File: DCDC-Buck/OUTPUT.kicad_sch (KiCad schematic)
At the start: 3 parts, among them CN2 STLZ950GH

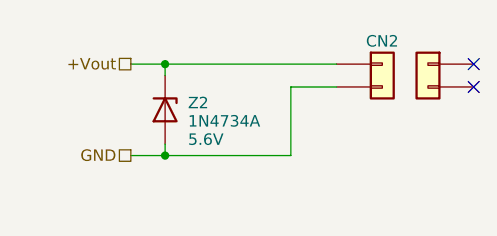
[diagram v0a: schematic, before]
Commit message: Finishing PCB design with 2 layers.
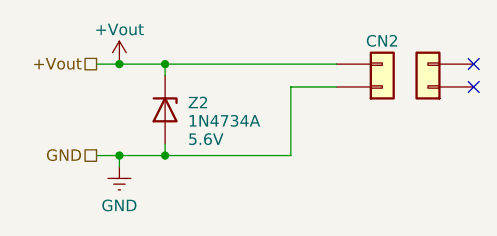
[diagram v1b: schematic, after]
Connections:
- net +Vout: now also CN2.2 (Pin_2); no longer CN2.1 (Pin_1)
- net GND: now also CN2.1 (Pin_1); no longer CN2.2 (Pin_2)
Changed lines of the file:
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@@
 	(title_block
 		(title "OUTPUT")
+		(date "2026-09-27")
 		(rev "A")
 		(company "Author: Ygor K.")
+	)
+	(junction
+		(at 125.73 96.52)
+		(diameter 0)
+		(color 0 0 0 0)
+	)
+	(junction
+		(at 125.73 106.68)
+		(diameter 0)
+		(color 0 0 0 0)
 	)
 	(junction
@@
 	(wire
 		(pts
-			(xy 127 96.52) (xy 130.81 96.52)
+			(xy 125.73 106.68) (xy 130.81 106.68)
+		)
+		(stroke
+			(width 0)
+			(type default)
+		)
+	)
+	(wire
+		(pts
+			(xy 123.19 96.52) (xy 125.73 96.52)
 		)
 		(stroke
@@
 	(wire
 		(pts
-			(xy 127 106.68) (xy 130.81 106.68)
+			(xy 125.73 96.52) (xy 130.81 96.52)
+		)
+		(stroke
+			(width 0)
+			(type default)
+		)
+	)
+	(wire
+		(pts
+			(xy 123.19 106.68) (xy 125.73 106.68)
+		)
+		(stroke
+			(width 0)
+			(type default)
+		)
+	)
+	(wire
+		(pts
+			(xy 125.73 106.68) (xy 125.73 107.95)
 		)
 		(stroke
@@
 	(hierarchical_label "+Vout"
 		(shape passive)
-		(at 127 96.52 180)
+		(at 123.19 96.52 180)
 		(effects
 			(font
@@
 	(hierarchical_label "GND"
 		(shape passive)
-		(at 127 106.68 180)
+		(at 123.19 106.68 180)
 		(effects
 			(font
@@
 	)
 	(symbol
+		(lib_id "power:VCC")
+		(at 125.73 96.52 0)
+		(unit 1)
+		(body_style 1)
+		(exclude_from_sim no)
+		(in_bom yes)
+		(on_board yes)
+		(in_pos_files yes)
+		(dnp no)
+		(property "Reference" "#PWR028"
+			(at 125.73 100.33 0)
+			(hide yes)
+			(show_name no)
+			(do_not_autoplace no)
+			(effects
+				(font
+					(size 1.27 1.27)
+				)
+			)
+		)
+		(property "Value" "+Vout"
+			(at 125.73 92.71 0)
+			(show_name no)
+			(do_not_autoplace no)
+			(effects
+				(font
+					(size 1.27 1.27)
+				)
+			)
+		)
+		(property "Footprint" ""
+			(at 125.73 96.52 0)
+			(hide yes)
+			(show_name no)
+			(do_not_autoplace no)
+			(effects
+				(font
+					(size 1.27 1.27)
+				)
+			)
+		)
+		(property "Datasheet" ""
+			(at 125.73 96.52 0)
+			(hide yes)
+			(show_name no)
+			(do_not_autoplace no)
+			(effects
+				(font
+					(size 1.27 1.27)
+				)
+			)
+		)
+		(property "Description" "Power symbol creates a global label with name \"VCC\""
+			(at 125.73 96.52 0)
+			(hide yes)
+			(show_name no)
+			(do_not_autoplace no)
+			(effects
+				(font
+					(size 1.27 1.27)
+				)
+			)
+		)
+		(pin "1"
+		)
+		(instances
+			(project "DCDC-Buck"
+				(path "/959e3d1c-01d0-4c7d-bf19-165b598aa596/74582b42-0ce4-4cfd-893d-1b8aeecfe42a"
+					(reference "#PWR028")
+					(unit 1)
+				)
+			)
+		)
+	)
+	(symbol
 		(lib_id "Connector_Generic:Conn_01x02")
-		(at 154.94 96.52 0)
+		(at 154.94 99.06 0)
+		(mirror x)
 		(unit 1)
 		(body_style 1)
@@
 		)
 		(property "Value" "STLZ950GH"
-			(at 154.94 102.108 0)
+			(at 154.94 93.472 0)
 			(hide yes)
 			(show_name no)
@@
 		)
 		(property "Footprint" "TerminalBlock_Phoenix:TerminalBlock_Phoenix_MKDS-1,5-2-5.08_1x02_P5.08mm_Horizontal"
-			(at 154.94 96.52 0)
+			(at 154.94 99.06 0)
 			(hide yes)
 			(show_name no)
@@
 		)
 		(property "Datasheet" ""
-			(at 154.94 96.52 0)
+			(at 154.94 99.06 0)
 			(hide yes)
 			(show_name no)
@@
 		)
 		(property "Description" "Conector Verde Multipolar STLZ950GH Macho 90º (Horizontal) Com as Laterais Fechadas - Passo 5,08mm"
-			(at 154.94 96.52 0)
+			(at 154.94 99.06 0)
 			(hide yes)
 			(show_name no)
@@
 		)
 		(property "Link" "https://www.multcomercial.com.br/conector-verde-multipolar-stlz950gh-macho-90-horizontal-com-as-laterais-fechadas-passo-5-08mm-2-a-18-vias-phoenix-mecano.html"
-			(at 154.94 96.52 0)
+			(at 154.94 99.06 0)
 			(hide yes)
 			(show_name no)
@@
 				(path "/959e3d1c-01d0-4c7d-bf19-165b598aa596/74582b42-0ce4-4cfd-893d-1b8aeecfe42a"
 					(reference "CN2")
+					(unit 1)
+				)
+			)
+		)
+	)
+	(symbol
+		(lib_id "power:GNDREF")
+		(at 125.73 107.95 0)
+		(unit 1)
+		(body_style 1)
+		(exclude_from_sim no)
+		(in_bom yes)
+		(on_board yes)
+		(in_pos_files yes)
+		(dnp no)
+		(property "Reference" "#PWR048"
+			(at 125.73 114.3 0)
+			(hide yes)
+			(show_name no)
+			(do_not_autoplace no)
+			(effects
+				(font
+					(size 1.27 1.27)
+				)
+			)
+		)
+		(property "Value" "GND"
+			(at 125.73 112.268 0)
+			(show_name no)
+			(do_not_autoplace no)
+			(effects
+				(font
+					(size 1.27 1.27)
+				)
+			)
+		)
+		(property "Footprint" ""
+			(at 125.73 107.95 0)
+			(hide yes)
+			(show_name no)
+			(do_not_autoplace no)
+			(effects
+				(font
+					(size 1.27 1.27)
+				)
+			)
+		)
+		(property "Datasheet" ""
+			(at 125.73 107.95 0)
+			(hide yes)
+			(show_name no)
+			(do_not_autoplace no)
+			(effects
+				(font
+					(size 1.27 1.27)
+				)
+			)
+		)
+		(property "Description" "Power symbol creates a global label with name \"GNDREF\" , reference supply ground"
+			(at 125.73 107.95 0)
+			(hide yes)
+			(show_name no)
+			(do_not_autoplace no)
+			(effects
+				(font
+					(size 1.27 1.27)
+				)
+			)
+		)
+		(pin "1"
+		)
+		(instances
+			(project "DCDC-Buck"
+				(path "/959e3d1c-01d0-4c7d-bf19-165b598aa596/74582b42-0ce4-4cfd-893d-1b8aeecfe42a"
+					(reference "#PWR048")
+					(unit 1)
+				)
+			)
+		)
+	)
+	(symbol
+		(lib_name "Conn_01x02_1")
+		(lib_id "Connector_Generic:Conn_01x02")
+		(at 160.02 99.06 180)
+		(unit 1)
+		(body_style 1)
+		(exclude_from_sim no)
+		(in_bom yes)
+		(on_board no)
+		(in_pos_files no)
+		(dnp no)
+		(property "Reference" "EXT2"
+			(at 160.02 101.6 0)
+			(hide yes)
+			(show_name no)
+			(do_not_autoplace no)
+			(effects
+				(font
+					(size 1.27 1.27)
+				)
+			)
+		)
+		(property "Value" "AKZ950"
+			(at 160.02 93.472 0)
+			(hide yes)
+			(show_name no)
+			(do_not_autoplace no)
+			(effects
+				(font
+					(size 1.27 1.27)
+				)
+			)
+		)
+		(property "Footprint" ""
+			(at 160.02 99.06 0)
+			(hide yes)
+			(show_name no)
+			(do_not_autoplace no)
+			(effects
+				(font
+					(size 1.27 1.27)
+				)
+			)
+		)
+		(property "Datasheet" ""
+			(at 160.02 99.06 0)
+			(hide yes)
+			(show_name no)
+			(do_not_autoplace no)
+			(effects
+				(font
+					(size 1.27 1.27)
+				)
+			)
+		)
+		(property "Description" "Conector Verde Multipolar AKZ950 Fêmea - Passo 5,08mm"
+			(at 160.02 99.06 0)
+			(hide yes)
+			(show_name no)
+			(do_not_autoplace no)
+			(effects
+				(font
+					(size 1.27 1.27)
+				)
+			)
+		)
+		(property "Link" "https://www.multcomercial.com.br/conector-verde-multipolar-akz950-femea-passo-5-08mm-phoenix-mecano.html"
+			(at 160.02 99.06 0)
+			(hide yes)
+			(show_name no)
+			(do_not_autoplace no)
+			(effects
+				(font
+					(size 1.27 1.27)
+				)
+			)
+		)
+		(pin "1"
+		)
+		(pin "2"
+		)
+		(instances
+			(project "DCDC-Buck"
+				(path "/959e3d1c-01d0-4c7d-bf19-165b598aa596/74582b42-0ce4-4cfd-893d-1b8aeecfe42a"
+					(reference "EXT2")
 					(unit 1)
 				)
@@
 					(unit 1)
 				)
-			)
-		)
-	)
-	(symbol
-		(lib_name "Conn_01x02_1")
-		(lib_id "Connector_Generic:Conn_01x02")
-		(at 160.02 96.52 0)
-		(mirror y)
-		(unit 1)
-		(body_style 1)
-		(exclude_from_sim no)
-		(in_bom yes)
-		(on_board no)
-		(in_pos_files no)
-		(dnp no)
-		(property "Reference" "EXT2"
-			(at 160.02 93.98 0)
-			(hide yes)
-			(show_name no)
-			(do_not_autoplace no)
-			(effects
-				(font
-					(size 1.27 1.27)
-				)
-			)
-		)
-		(property "Value" "AKZ950"
-			(at 160.02 102.108 0)
-			(hide yes)
-			(show_name no)
-			(do_not_autoplace no)
-			(effects
-				(font
-					(size 1.27 1.27)
-				)
-			)
-		)
-		(property "Footprint" ""
-			(at 160.02 96.52 0)
-			(hide yes)
-			(show_name no)
-			(do_not_autoplace no)
-			(effects
-				(font
-					(size 1.27 1.27)
-				)
-			)
-		)
-		(property "Datasheet" ""
-			(at 160.02 96.52 0)
-			(hide yes)
-			(show_name no)
-			(do_not_autoplace no)
-			(effects
-				(font
-					(size 1.27 1.27)
-				)
-			)
-		)
-		(property "Description" "Conector Verde Multipolar AKZ950 Fêmea - Passo 5,08mm"
-			(at 160.02 96.52 0)
-			(hide yes)
-			(show_name no)
-			(do_not_autoplace no)
-			(effects
-				(font
-					(size 1.27 1.27)
-				)
-			)
-		)
-		(property "Link" "https://www.multcomercial.com.br/conector-verde-multipolar-akz950-femea-passo-5-08mm-phoenix-mecano.html"
-			(at 160.02 96.52 0)
-			(hide yes)
-			(show_name no)
-			(do_not_autoplace no)
-			(effects
-				(font
-					(size 1.27 1.27)
-				)
-			)
-		)
-		(pin "1"
-		)
-		(pin "2"
-		)
-		(instances
-			(project "DCDC-Buck"
-				(path "/959e3d1c-01d0-4c7d-bf19-165b598aa596/74582b42-0ce4-4cfd-893d-1b8aeecfe42a"
-					(reference "EXT2")
-					(unit 1)
-				)
